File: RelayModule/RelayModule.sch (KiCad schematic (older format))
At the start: 10 parts

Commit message: Esquema en proceso
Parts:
- added JP1: Jumper_NO_Small, symbol Jumper_NO_Small
- added R1: 1k, symbol R
- D1: renamed from D?; value LED -> LED_POWER
- D2: renamed from D?; value LED -> LED_ON
- P1: renamed from P?; value CONN_01X03 -> Control_connector
- P2: renamed from P?; value CONN_01X03 -> Power_connector
- gave numbers to parts that had none: 6
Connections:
- wire segments 13 -> 39
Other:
- moved on the sheet: D1, D2, D3, P1, P2, Q1, R2, R3, RELAY1, U1

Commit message: Esquema terminado
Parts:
- D3: value DIODE -> 1N4148
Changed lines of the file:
@@
 LIBS:рэс-49
 LIBS:тпг-1
+LIBS:RelayModule-cache
 EELAYER 25 0
 EELAYER END
@@
 P 6550 3600
 F 0 "D3" H 6550 3700 50  0000 C CNN
-F 1 "DIODE" H 6550 3500 50  0000 C CNN
+F 1 "1N4148" H 6550 3500 50  0000 C CNN
 F 2 "" H 6550 3600 60  0000 C CNN
 F 3 "" H 6550 3600 60  0000 C CNN

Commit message: Placa terminada, V1.0
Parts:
- D1, D2: footprint (none) -> LEDs:LED_0805
- D3: footprint (none) -> Diodes_SMD:D_SOD-123
- JP1: footprint (none) -> Pin_Headers:Pin_Header_Straight_1x02_Pitch2.54mm
- P1: footprint (none) -> Connectors_JST:JST_PH_S3B-PH-K_03x2.00mm_Angled
- P2: footprint (none) -> SparkFun-Connectors:SCREWTERMINAL-5MM-3
- Q1: footprint TO-92 -> TO_SOT_Packages_SMD:SOT-23
- R1, R2, R3: footprint (none) -> Resistors_SMD:R_0805
- RELAY1: footprint (none) -> Relays_THT:Relay_SANYOU_SRD_Series_Form_C
- U1: footprint DIP-4 -> Housings_DIP:DIP-4_W7.62mm
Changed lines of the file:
@@
 F 0 "U1" H 5150 4250 50  0000 L CNN
 F 1 "PC817" H 5350 4250 50  0000 L CNN
-F 2 "DIP-4" H 5150 3850 50  0001 L CIN
+F 2 "Housings_DIP:DIP-4_W7.62mm" H 5150 3850 50  0001 L CIN
 F 3 "" H 5350 4050 50  0001 L CNN
 	1    5350 4050
@@
 F 0 "R2" V 4830 3950 50  0000 C CNN
 F 1 "1k" V 4750 3950 50  0000 C CNN
-F 2 "" V 4680 3950 50  0001 C CNN
+F 2 "Resistors_SMD:R_0805" V 4680 3950 50  0001 C CNN
 F 3 "" H 4750 3950 50  0001 C CNN
 	1    4750 3950
@@
 F 0 "P1" H 2700 3900 50  0000 C CNN
 F 1 "Control_connector" V 2800 3700 50  0000 C CNN
-F 2 "" H 2700 3700 50  0001 C CNN
+F 2 "Connectors_JST:JST_PH_S3B-PH-K_03x2.00mm_Angled" H 2700 3700 50  0001 C CNN
 F 3 "" H 2700 3700 50  0001 C CNN
 	1    2700 3700
@@
 F 0 "RELAY1" H 7800 5150 60  0000 C CNN
 F 1 "SONGLE_RELAY" V 7100 4950 60  0000 C CNN
-F 2 "" H 7450 4250 60  0001 C CNN
+F 2 "Relays_THT:Relay_SANYOU_SRD_Series_Form_C" H 7450 4250 60  0001 C CNN
 F 3 "" H 7450 4250 60  0001 C CNN
 	1    7450 4250
@@
 F 0 "Q1" H 6650 4225 50  0000 L CNN
 F 1 "S8050" H 6650 4150 50  0000 L CNN
-F 2 "TO-92" H 6650 4075 50  0001 L CIN
+F 2 "TO_SOT_Packages_SMD:SOT-23" H 6650 4075 50  0001 L CIN
 F 3 "" H 6450 4150 50  0001 L CNN
 	1    6450 4150
@@
 F 0 "D2" H 4450 4250 50  0000 C CNN
 F 1 "LED_ON" H 4450 4050 50  0000 C CNN
-F 2 "" H 4450 4150 50  0001 C CNN
+F 2 "LEDs:LED_0805" H 4450 4150 50  0001 C CNN
 F 3 "" H 4450 4150 50  0001 C CNN
 	1    4450 4150
@@
 F 0 "D3" H 6550 3700 50  0000 C CNN
 F 1 "1N4148" H 6550 3500 50  0000 C CNN
-F 2 "" H 6550 3600 60  0000 C CNN
+F 2 "Diodes_SMD:D_SOD-123" H 6550 3600 60  0001 C CNN
 F 3 "" H 6550 3600 60  0000 C CNN
 	1    6550 3600
@@
 F 0 "P2" H 8800 3750 50  0000 C CNN
 F 1 "Power_connector" V 8900 3550 50  0000 C CNN
-F 2 "" H 8800 3550 50  0001 C CNN
+F 2 "SparkFun-Connectors:SCREWTERMINAL-5MM-3" H 8800 3550 50  0001 C CNN
 F 3 "" H 8800 3550 50  0001 C CNN
 	1    8800 3550
@@
 F 0 "D1" H 3700 3800 50  0000 C CNN
 F 1 "LED_POWER" H 3700 3600 50  0000 C CNN
-F 2 "" H 3700 3700 50  0001 C CNN
+F 2 "LEDs:LED_0805" H 3700 3700 50  0001 C CNN
 F 3 "" H 3700 3700 50  0001 C CNN
 	1    3700 3700
@@
 F 0 "R3" V 6030 4150 50  0000 C CNN
 F 1 "510" V 5950 4150 50  0000 C CNN
-F 2 "" V 5880 4150 50  0001 C CNN
+F 2 "Resistors_SMD:R_0805" V 5880 4150 50  0001 C CNN
 F 3 "" H 5950 4150 50  0001 C CNN
 	1    5950 4150
@@
 F 0 "JP1" H 5300 3330 50  0000 C CNN
 F 1 "Jumper_NO_Small" H 5310 3190 50  0000 C CNN
-F 2 "" H 5300 3250 50  0001 C CNN
+F 2 "Pin_Headers:Pin_Header_Straight_1x02_Pitch2.54mm" H 5300 3250 50  0001 C CNN
 F 3 "" H 5300 3250 50  0001 C CNN
 	1    5300 3250
@@
 F 0 "R1" V 3780 3300 50  0000 C CNN
 F 1 "1k" V 3700 3300 50  0000 C CNN
-F 2 "" V 3630 3300 50  0001 C CNN
+F 2 "Resistors_SMD:R_0805" V 3630 3300 50  0001 C CNN
 F 3 "" H 3700 3300 50  0001 C CNN
 	1    3700 3300

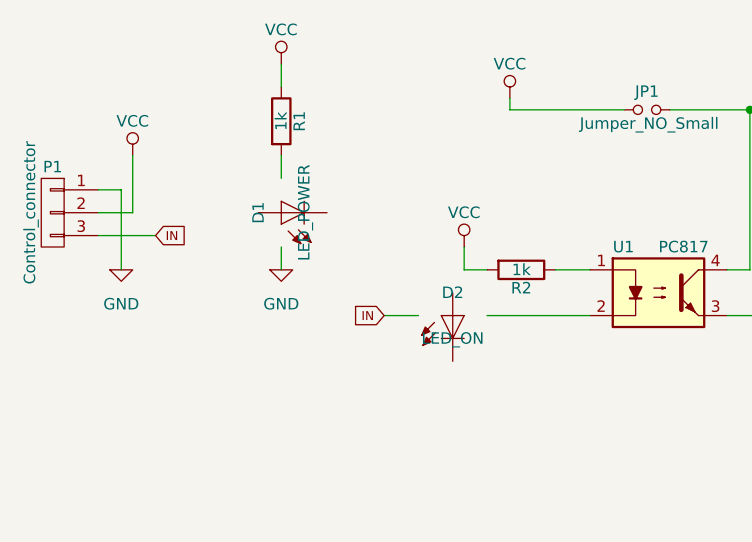
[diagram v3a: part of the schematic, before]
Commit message: Conector cambiado
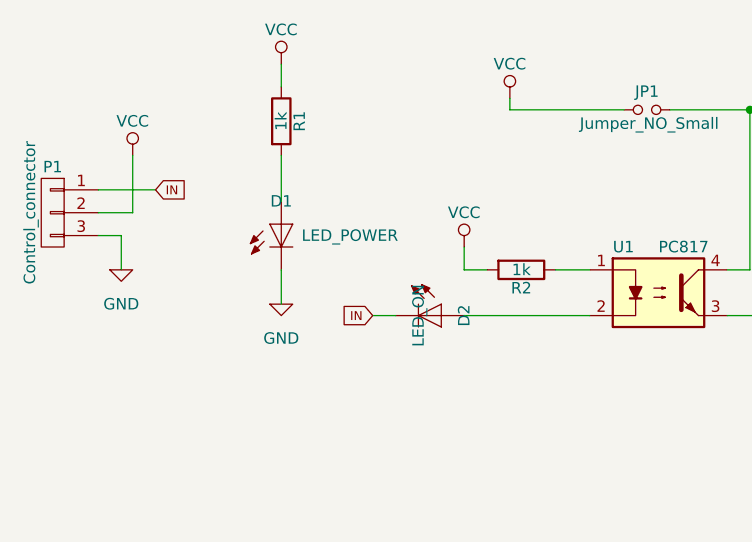
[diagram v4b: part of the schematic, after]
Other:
- moved on the sheet: D1, D2
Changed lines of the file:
@@
 EESchema Schematic File Version 2
-LIBS:power
-LIBS:device
-LIBS:transistors
-LIBS:conn
-LIBS:linear
-LIBS:regul
+LIBS:74xgxx
 LIBS:74xx
-LIBS:cmos4000
-LIBS:adc-dac
-LIBS:memory
-LIBS:xilinx
-LIBS:microcontrollers
-LIBS:dsp
-LIBS:microchip
-LIBS:analog_switches
-LIBS:motorola
-LIBS:texas
-LIBS:intel
-LIBS:audio
-LIBS:interface
-LIBS:digital-audio
-LIBS:philips
-LIBS:display
-LIBS:cypress
-LIBS:siliconi
-LIBS:opto
-LIBS:atmel
-LIBS:contrib
-LIBS:valves
-LIBS:74xgxx
 LIBS:5050_ws2811
 LIBS:a4988-module
@@
 LIBS:actel
 LIBS:adafruit
+LIBS:adc-dac
 LIBS:adxl345
 LIBS:allegro
@@
 LIBS:AMS1117
 LIBS:analog_devices
+LIBS:analog_switches
 LIBS:ant
 LIBS:at24c64
+LIBS:atmel
+LIBS:audio
 LIBS:battery_management
 LIBS:bbd
@@
 LIBS:bosch
 LIBS:brooktre
+LIBS:cmos4000
 LIBS:cmos_ieee
+LIBS:conn
+LIBS:contrib
 LIBS:cp2103
 LIBS:CP2102
+LIBS:cypress
 LIBS:dc-dc
+LIBS:device
 LIBS:dht11
+LIBS:digital-audio
 LIBS:diode
+LIBS:display
+LIBS:dsp
 LIBS:elec-unifil
 LIBS:er-oled-ssd1306
@@
 LIBS:HC164
 LIBS:hlk-rm04
+LIBS:intel
+LIBS:interface
 LIBS:ir
 LIBS:irf7907
@@
 LIBS:Lattice
 LIBS:LilyPad-Wearables
+LIBS:linear
 LIBS:LM2575
 LIBS:logo
@@
 LIBS:MCP3208
 LIBS:mechanical
+LIBS:memory
+LIBS:microchip
 LIBS:microchip_dspic33dsc
 LIBS:microchip_pic10mcu
@@
 LIBS:microchip_pic18mcu
 LIBS:microchip_pic32mcu
+LIBS:microcontrollers
 LIBS:miniusb
 LIBS:motor_drivers
+LIBS:motorola
 LIBS:motors
 LIBS:mp2109dq
@@
 LIBS:OF5032
 LIBS:onsemi
+LIBS:opto
 LIBS:Oscillators
+LIBS:philips
 LIBS:pl2303
 LIBS:pogopin
+LIBS:power
 LIBS:powerint
 LIBS:powerjack
@@
 LIBS:pt4115
 LIBS:references
+LIBS:regul
 LIBS:relays
 LIBS:rfcom
@@
 LIBS:sensors
 LIBS:silabs
+LIBS:siliconi
 LIBS:smd oscillator
 LIBS:songle_relay
@@
 LIBS:Teensy_3_and_LC_Series_Boards_v1.1
 LIBS:test
+LIBS:texas
 LIBS:texas-msp
 LIBS:tlv70233
 LIBS:tp4056
 LIBS:transf
+LIBS:transistors
 LIBS:ts812c
 LIBS:ttl_ieee
@@
 LIBS:usb_ax2
 LIBS:User-Submitted
+LIBS:valves
 LIBS:video
 LIBS:w25q32bv
@@
 LIBS:XC9572-TQ100
 LIBS:Xicor
+LIBS:xilinx
 LIBS:xilinx_spartan3_virtex4_and_5
 LIBS:zetex
@@
 L LED D2
 U 1 1 592C0519
-P 4450 4150
-F 0 "D2" H 4450 4250 50  0000 C CNN
-F 1 "LED_ON" H 4450 4050 50  0000 C CNN
-F 2 "LEDs:LED_0805" H 4450 4150 50  0001 C CNN
-F 3 "" H 4450 4150 50  0001 C CNN
-	1    4450 4150
-	1    0    0    -1
+P 4400 4150
+F 0 "D2" H 4400 4250 50  0000 C CNN
+F 1 "LED_ON" H 4400 4050 50  0000 C CNN
+F 2 "LEDs:LED_0805" H 4400 4150 50  0001 C CNN
+F 3 "" H 4400 4150 50  0001 C CNN
+	1    4400 4150
+	0    1    1    0
 $EndComp
 $Comp
@@
 $EndComp
 Wire Wire Line
-	2900 3600 3000 3600
-Wire Wire Line
-	3000 3600 3000 3950
+	2900 3600 3150 3600
 $Comp
 L LED D1
 U 1 1 592C1895
-P 3700 3700
-F 0 "D1" H 3700 3800 50  0000 C CNN
-F 1 "LED_POWER" H 3700 3600 50  0000 C CNN
-F 2 "LEDs:LED_0805" H 3700 3700 50  0001 C CNN
-F 3 "" H 3700 3700 50  0001 C CNN
-	1    3700 3700
-	0    -1   -1   0
-$EndComp
-Wire Wire Line
-	2900 3800 3150 3800
-Text GLabel 3150 3800 2    39   Input ~ 0
+P 3700 3750
+F 0 "D1" H 3700 3850 50  0000 C CNN
+F 1 "LED_POWER" H 4000 3700 50  0000 C CNN
+F 2 "LEDs:LED_0805" H 3700 3750 50  0001 C CNN
+F 3 "" H 3700 3750 50  0001 C CNN
+	1    3700 3750
+	1    0    0    -1
+$EndComp
+Text GLabel 3150 3600 2    39   Input ~ 0
 IN
 Wire Wire Line
@@
 	4500 3950 4600 3950
 Wire Wire Line
-	4600 4150 5050 4150
-Text GLabel 4150 4150 0    39   Input ~ 0
+	4500 4150 5050 4150
+Text GLabel 4100 4150 0    39   Input ~ 0
 IN
-Wire Wire Line
-	4150 4150 4300 4150
 Wire Wire Line
 	6550 4350 6550 4500
@@
 L GND #PWR06
 U 1 1 592C3895
-P 3700 3950
-F 0 "#PWR06" H 3700 3700 50  0001 C CNN
-F 1 "GND" H 3700 3800 50  0000 C CNN
-F 2 "" H 3700 3950 50  0001 C CNN
-F 3 "" H 3700 3950 50  0001 C CNN
-	1    3700 3950
+P 3700 4100
+F 0 "#PWR06" H 3700 3850 50  0001 C CNN
+F 1 "GND" H 3700 3950 50  0000 C CNN
+F 2 "" H 3700 4100 50  0001 C CNN
+F 3 "" H 3700 4100 50  0001 C CNN
+	1    3700 4100
 	1    0    0    -1
 $EndComp
@@
 	3700 3050 3700 3150
 Wire Wire Line
-	3700 3450 3700 3550
-Wire Wire Line
-	3700 3850 3700 3950
+	3700 3450 3700 3650
 Wire Wire Line
 	8050 3550 8600 3550
@@
 	1    0    0    -1
 $EndComp
+Wire Wire Line
+	3700 3950 3700 4100
+Wire Wire Line
+	2900 3800 3000 3800
+Wire Wire Line
+	3000 3800 3000 3950
+Wire Wire Line
+	4100 4150 4200 4150
 $EndSCHEMATC
